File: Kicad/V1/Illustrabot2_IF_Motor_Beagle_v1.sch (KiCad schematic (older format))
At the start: 76 parts

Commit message: Update :  - Missing resistor value  - pins on beaglebone to define  - double motor supply
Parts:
- removed C? (x2): 100uF, ~, symbol CP
- removed JP? (x4): JUMPER3, ~, symbol JUMPER3
- removed K? (x6): CONN_3, ~, symbol CONN_3
- removed P? (x16): CONN_2, symbol CONN_2
- removed U? (x2): STEPSTICK, ~, symbol STEPSTICK
- added C10, C11, C12, C13, C14, C9: 100nF, ~, symbol C
- added C4, C5: 100uF, ~, symbol CP
- added JP11, JP13, JP7, JP9: JUMPER3, ~, symbol JUMPER3
- added P1, P10, P2, P3, P4, P5, P6, P7, P8, P9: CONN_4, symbol CONN_4
- added R1, R10, R12, R2, R3, R4: 10k, ~, symbol R
- added U3, U5: STEPSTICK, ~, symbol STEPSTICK
- C1, C2: renamed from C?; value C -> 10uF
- gave numbers to parts that had none: 44
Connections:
- net labels added: Beaglebone_3.3V, Beaglebone_5V, Direction_m1, Direction_m2, Direction_m3, Direction_m4, Position_m1, Position_m2, Position_m3, Position_m4, Position_m5, Position_m6, Step_m1, direction_m1, direction_m2, direction_m3, direction_m4, direction_m5, direction_m6, step_m1, step_m2, step_m3, step_m4, step_m5, step_m6
- net labels removed: Beaglebone 3.3V, Beaglebone 5V, Position_motor1, Position_motor2, Position_motor3, Position_motor4, Position_motor5, Position_motor6
- wire segments 278 -> 342
- no-connect marks 0 -> 66
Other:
- note added: "Nota : Tracks need \nto support 12A"
- note removed: "Nota : Tracks need to support 12A"
- moved on the sheet: C3, C7, JP1, JP10, JP3, JP8, P11, P12, U1, U4

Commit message: Update
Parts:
- removed C11, C12: 100nF, ~, symbol C
- removed C3, C4, C5: 100uF, ~, symbol CP
- removed JP1, JP10, JP11, JP12, JP13, JP14, JP2, JP3, JP4, JP5, JP7, JP8, JP9: JUMPER3, ~, symbol JUMPER3
- removed P2, P4, P9: CONN_4, symbol CONN_4
- added C1, C11, C12: 100uF, symbol CP
- added C10, C5: 100nF, symbol C
- added JP2, JP3, JP4, JP5, JP6, JP7: JUMPER, symbol JUMPER
- added P1, P5, P8: CONN_4, symbol CONN_4
- added RR1: RR8, symbol RR8
- C13, C14, C7, C8, C9, D1, D2, D3, D4, D5, D6, R1, R10, R12, R2, R3, R4, U1, U2, U3, U4, U5, U6: footprint ~ -> (none)
- C2: renamed from C6; footprint ~ -> (none)
- C3: renamed from C2; footprint ~ -> (none)
- C4: renamed from C1; footprint ~ -> (none)
- C6: renamed from C10; footprint ~ -> (none)
- JP1: renamed from JP6; footprint ~ -> (none)
- Q1, Q2, Q3, Q4, Q5, Q6: footprint ~ -> TO92
- R11, R14, R16, R18, R6, R8: value R -> 82k; footprint ~ -> (none)
- R13, R15, R17, R5, R7, R9: value 330 -> 150; footprint ~ -> (none)
- renumbered P3 to P2, P1 to P3, P5 to P4, P8 to P9
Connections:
- net labels added: Direction_m5, Direction_m6, Step_m2, Step_m3, Step_m4, Step_m5, Step_m6, ms1_m1, ms1_m2, ms1_m3, ms1_m4, ms1_m5, ms1_m6, ms2_m1, ms2_m2, ms2_m3, ms2_m4, ms2_m5, ms2_m6
- net labels removed: +24V, Beaglebone_3.3V, External 24V, GNDA
- wire segments 342 -> 313
- no-connect marks 66 -> 64
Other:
- moved on the sheet: C2, C3, C4, C6, JP1, P11, P12, P2, P3, P4, R2, U2

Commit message: Footprint association Component placing
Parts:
- removed RR1: RR8, symbol RR8
- added R19, R20, R21, R22, R23, R24: 10kohm, R3, symbol R
- C1, C11, C12, C2, C7, C8: footprint (none) -> CP4
- C10, C13, C14, C3, C4, C5, C6, C9: footprint (none) -> C1
- D1, D2, D3, D4, D5, D6: footprint (none) -> LED-3MM
- JP1: footprint (none) -> SIL-3
- JP2, JP3, JP4, JP5, JP6, JP7: footprint (none) -> SIL-2
- P1, P10, P2, P3, P4, P5, P6, P7: footprint (none) -> bornier4
- P11: renamed from P9; footprint (none) -> bornier4
- P12: renamed from P8; footprint (none) -> bornier4
- P8: renamed from P12; footprint (none) -> SIL-2x23-v1
- P9: renamed from P11; footprint (none) -> SIL-2x23-v1
- R1, R10, R12, R2, R3, R4: value 10k -> 10kohm; footprint (none) -> R3
- R11, R14, R16, R18, R6, R8: value 82k -> 82kohm; footprint (none) -> R3
- R13, R15, R17, R5, R7, R9: value 150 -> 150ohm; footprint (none) -> R3
- U1, U2, U3, U4, U5, U6: footprint (none) -> Stepstick_footprint
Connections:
- net 3V3: now also R19.1, R20.1, R21.1, R22.1, R23.1, R24.1
- net 1B_M1: now reaches P2.4 (P4), U2.11 (1B)
- net 1A_M1: now reaches P2.3 (P3), U2.12 (1A)
- net 2A_M1: now reaches P2.2 (P2), U2.13 (2A)
- net 2B_M1: now reaches P2.1 (P1), U2.14 (2B)
- net 1B_M2: now reaches P6.4 (P4), U4.11 (1B)
- net 1A_M2: now reaches P6.3 (P3), U4.12 (1A)
- net 2A_M2: now reaches P6.2 (P2), U4.13 (2A)
- net 2B_M2: now reaches P6.1 (P1), U4.14 (2B)
- net 1B_M3: now reaches P12.4 (P4), U6.11 (1B)
- net 1A_M3: now reaches P12.3 (P3), U6.12 (1A)
- net 2A_M3: now reaches P12.2 (P2), U6.13 (2A)
- net 2B_M3: now reaches P12.1 (P1), U6.14 (2B)
- net 1B_M4: now reaches P1.4 (P4), U1.11 (1B)
- net 1A_M4: now reaches P1.3 (P3), U1.12 (1A)
- net 2A_M4: now reaches P1.2 (P2), U1.13 (2A)
- net 2B_M4: now reaches P1.1 (P1), U1.14 (2B)
- net 1B_M5: now reaches P5.4 (P4), U3.11 (1B)
- net 1A_M5: now reaches P5.3 (P3), U3.12 (1A)
- net 2A_M5: now reaches P5.2 (P2), U3.13 (2A)
- net 2B_M5: now reaches P5.1 (P1), U3.14 (2B)
- net 1B_M6: now reaches P7.4 (P4), U5.11 (1B)
- net 1A_M6: now reaches P7.3 (P3), U5.12 (1A)
- net 2A_M6: now reaches P7.2 (P2), U5.13 (2A)
- net 2B_M6: now reaches P7.1 (P1), U5.14 (2B)
- net ms1_m1: no longer names the net of JP3.1, U2.2 (MS1)
- net ms1_m1: now also R20.2
- net ms1_m2: no longer names the net of JP5.1, U4.2 (MS1)
- net ms1_m2: now also R22.2
- net ms1_m3: no longer names the net of JP7.1, U6.2 (MS1)
- net ms1_m3: now also R24.2
- net ms1_m4: no longer names the net of JP2.1, U1.2 (MS1)
- net ms1_m4: now also R19.2
- net ms1_m5: no longer names the net of JP4.1, U3.2 (MS1)
- net ms1_m5: now also R21.2
- net ms1_m6: no longer names the net of JP6.1, U5.2 (MS1)
- net ms1_m6: now also R23.2
- no-connect marks 64 -> 62
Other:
- moved on the sheet: JP2, JP3, JP4, JP5, JP6, JP7

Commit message: Routing
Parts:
- removed JP2, JP3, JP4, JP5, JP6, JP7: JUMPER, SIL-2, symbol JUMPER
- removed R19, R20, R21, R22, R23, R24: 10kohm, R3, symbol R
- added C15, C16, C17, C18, C19, C20: 10uF, C1, symbol C
- added P13, P14, P15, P16: CONN_1, 1pin, symbol CONN_1
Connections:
- net Direction_m1 is gone; now on net Direction_m4: U2.8 (Direction)
- net +12V: now also P4.2 (P2); no longer C11.1, C2.1, C7.1, P4.3 (P3), P4.4 (P4), U2.16 (Vmot), U3.16 (Vmot), U5.16 (Vmot)
- net +5V: now also C4.2; no longer C4.1
- net 1A_M1: now also P1.2 (P2), U1.12 (1A); no longer P2.3 (P3), U2.12 (1A)
- net 1A_M2: now also P12.2 (P2), U6.12 (1A); no longer P6.3 (P3), U4.12 (1A)
- net 1A_M3: now also P6.2 (P2), U4.12 (1A); no longer P12.3 (P3), U6.12 (1A)
- net 1A_M4: now also P2.2 (P2), U2.12 (1A); no longer P1.3 (P3), U1.12 (1A)
- net 1A_M5: now also P5.2 (P2); no longer P5.3 (P3)
- net 1A_M6: now also P7.2 (P2); no longer P7.3 (P3)
- net 1B_M1: now also P1.1 (P1), U1.11 (1B); no longer P2.4 (P4), U2.11 (1B)
- net 1B_M2: now also P12.1 (P1), U6.11 (1B); no longer P6.4 (P4), U4.11 (1B)
- net 1B_M3: now also P6.1 (P1), U4.11 (1B); no longer P12.4 (P4), U6.11 (1B)
- net 1B_M4: now also P2.1 (P1), U2.11 (1B); no longer P1.4 (P4), U1.11 (1B)
- net 1B_M5: now also P5.1 (P1); no longer P5.4 (P4)
- net 1B_M6: now also P7.1 (P1); no longer P7.4 (P4)
- net 2A_M1: now also P1.3 (P3), U1.13 (2A); no longer P2.2 (P2), U2.13 (2A)
- net 2A_M2: now also P12.3 (P3), U6.13 (2A); no longer P6.2 (P2), U4.13 (2A)
- net 2A_M3: now also P6.3 (P3), U4.13 (2A); no longer P12.2 (P2), U6.13 (2A)
- net 2A_M4: now also P2.3 (P3), U2.13 (2A); no longer P1.2 (P2), U1.13 (2A)
- net 2A_M5: now also P5.3 (P3); no longer P5.2 (P2)
- net 2A_M6: now also P7.3 (P3); no longer P7.2 (P2)
- net 2B_M1: now also P1.4 (P4), U1.14 (2B); no longer P2.1 (P1), U2.14 (2B)
- net 2B_M2: now also P12.4 (P4), U6.14 (2B); no longer P6.1 (P1), U4.14 (2B)
- net 2B_M3: now also P6.4 (P4), U4.14 (2B); no longer P12.1 (P1), U6.14 (2B)
- net 2B_M4: now also P2.4 (P4), U2.14 (2B); no longer P1.1 (P1), U1.14 (2B)
- net 2B_M5: now also P5.4 (P4); no longer P5.1 (P1)
- net 2B_M6: now also P7.4 (P4); no longer P7.1 (P1)
- net 3V3: now also C15.2, C16.2, C17.2, C18.2, C19.2, C20.2
- net AGND: no longer C11.2, C2.2, C7.2, P4.2 (P2), U2.15 (GND), U3.15 (GND), U5.15 (GND)
- net Beaglebone_5V: now also JP1.3; no longer JP1.1
- net Direction_m2: now also U6.8 (Direction); no longer U4.8 (Direction)
- net Direction_m3: now also U4.8 (Direction); no longer U6.8 (Direction)
- net Direction_m4: no longer U1.8 (Direction)
- net External 5V: now also JP1.1, P3.2 (P2); no longer JP1.3, P3.1 (P1)
- net GND: now also C4.1, P3.1 (P1), U1.2 (MS1), U2.2 (MS1), U3.2 (MS1), U4.2 (MS1), U5.2 (MS1), U6.2 (MS1), C15.1, C16.1, C17.1, C18.1, C19.1, C20.1, P13.1, P14.1, P15.1, P16.1; no longer C4.2, P3.2 (P2)
- net Step_m1: now also U1.7 (Step); no longer U2.7 (Step)
- net Step_m2: now also U6.7 (Step); no longer U4.7 (Step)
- net Step_m3: now also U4.7 (Step); no longer U6.7 (Step)
- net Step_m4: now also U2.7 (Step); no longer U1.7 (Step)
- net direction_m1: now also P8.8 (P8), U1.8 (Direction); no longer P8.7 (P7)
- net direction_m2: now also P8.14 (P14); no longer P8.13 (P13)
- net direction_m3: now also P8.17 (P17); no longer P8.18 (P18)
- net direction_m4: now also P8.11 (P11); no longer P8.12 (P12)
- net ms2_m1: now also P8.12 (P12), U1.3 (MS2); no longer P8.11 (P11), U2.3 (MS2)
- net ms2_m2: now also P8.18 (P18), U6.3 (MS2); no longer P8.17 (P17), U4.3 (MS2)
- net ms2_m3: now also P8.13 (P13), U4.3 (MS2); no longer P8.14 (P14), U6.3 (MS2)
- net ms2_m4: now also P8.7 (P7), U2.3 (MS2); no longer P8.8 (P8), U1.3 (MS2)
- net step_m1: now also P8.10 (P10); no longer P8.9 (P9)
- net step_m2: now also P8.16 (P16); no longer P8.15 (P15)
- net step_m3: now also P8.15 (P15); no longer P8.16 (P16)
- net step_m4: now also P8.9 (P9); no longer P8.10 (P10)
- new net +12C: C11.1, C2.1, C7.1, P4.4 (P4), U2.16 (Vmot), U3.16 (Vmot), U5.16 (Vmot)
- new net GNDA: C11.2, C2.2, C7.2, P4.3 (P3), U2.15 (GND), U3.15 (GND), U5.15 (GND)
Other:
- moved on the sheet: C3, C4, JP1

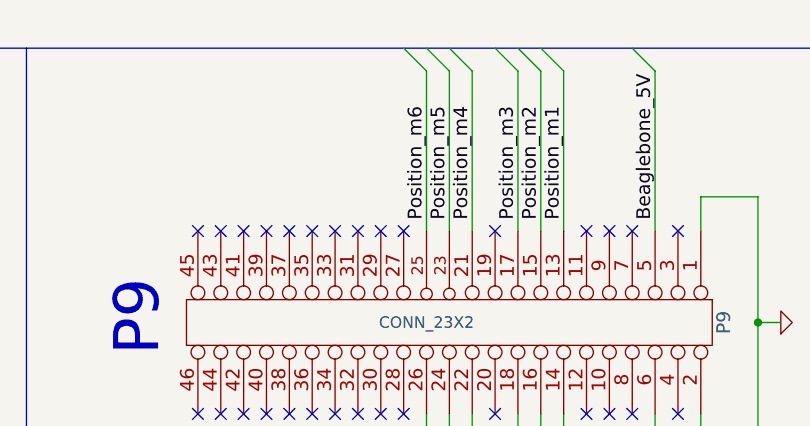
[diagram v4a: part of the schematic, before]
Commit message: Modification P9 header (pin 25 -> pin 27)
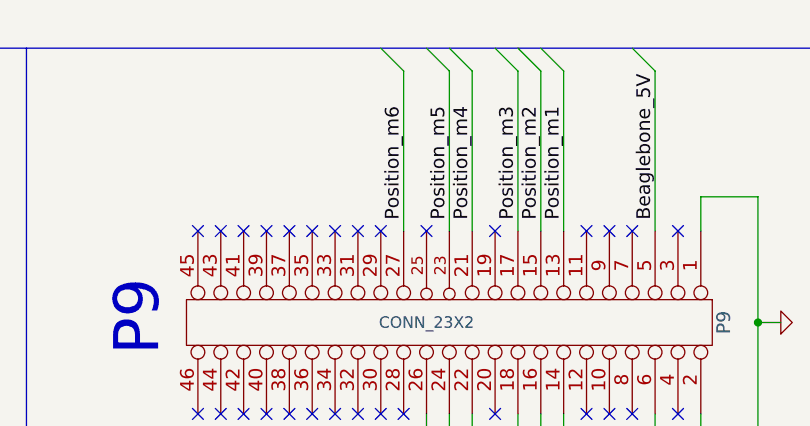
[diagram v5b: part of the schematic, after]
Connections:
- net Position_m6: now also P9.27 (P27); no longer P9.25 (P25)
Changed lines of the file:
@@
 Sheet 1 1
 Title "Carte Interface Beaglebone / Bras robotisé"
-Date "11 feb 2014"
+Date "15 mar 2014"
 Rev "1.0"
 Comp "Fablab Lannion"
@@
 NoConn ~ 13850 1400
 NoConn ~ 13950 1400
-NoConn ~ 14050 1400
 NoConn ~ 14450 1400
 NoConn ~ 14850 1400
@@
 	14150 600  14250 700
 Entry Wire Line
-	14050 600  14150 700
+	13950 600  14050 700
 Text Label 14750 1350 1    60   ~ 0
 Position_m1
@@
 Text Label 14250 1350 1    60   ~ 0
 Position_m5
-Text Label 14150 1350 1    60   ~ 0
+Text Label 14050 1350 1    60   ~ 0
 Position_m6
 Entry Wire Line
@@
 Wire Wire Line
 	14250 1400 14250 700
-Wire Wire Line
-	14150 1400 14150 700
 Wire Wire Line
 	14750 2200 14750 3000
@@
 	1750 1000 1800 1000
 Connection ~ 1800 1000
+Wire Wire Line
+	14050 1400 14050 700
+NoConn ~ 14150 1400
 $EndSCHEMATC
